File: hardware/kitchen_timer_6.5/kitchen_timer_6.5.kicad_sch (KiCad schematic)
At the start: 58 parts, among them J1 JST PH 2.0, J2 USB_C, J3 BREAKOUT, Q1 MMBT2222A, Q2 MMBT2222A, Q3 MMBT2222A, Q4 MMBT2222A, Q5 MMBT2222A, SW1 ON/OFF, SW2 SECONDS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

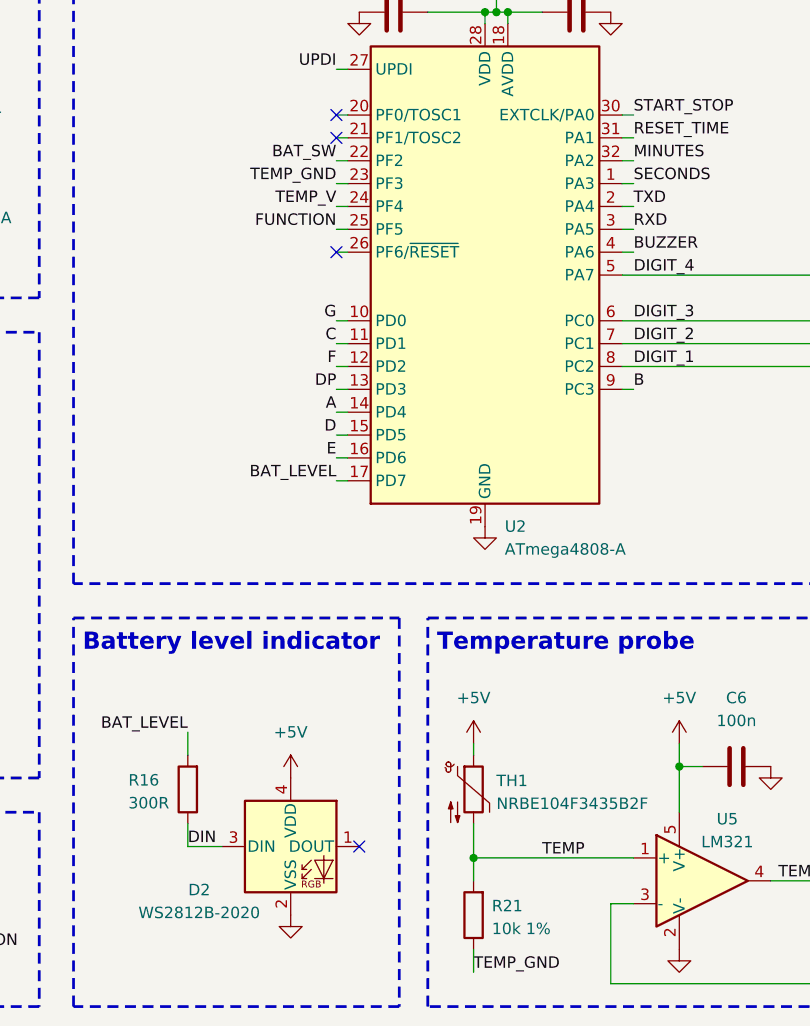
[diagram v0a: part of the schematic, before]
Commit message: converted temp_gnd to temp_vcc and change temperature reading logic
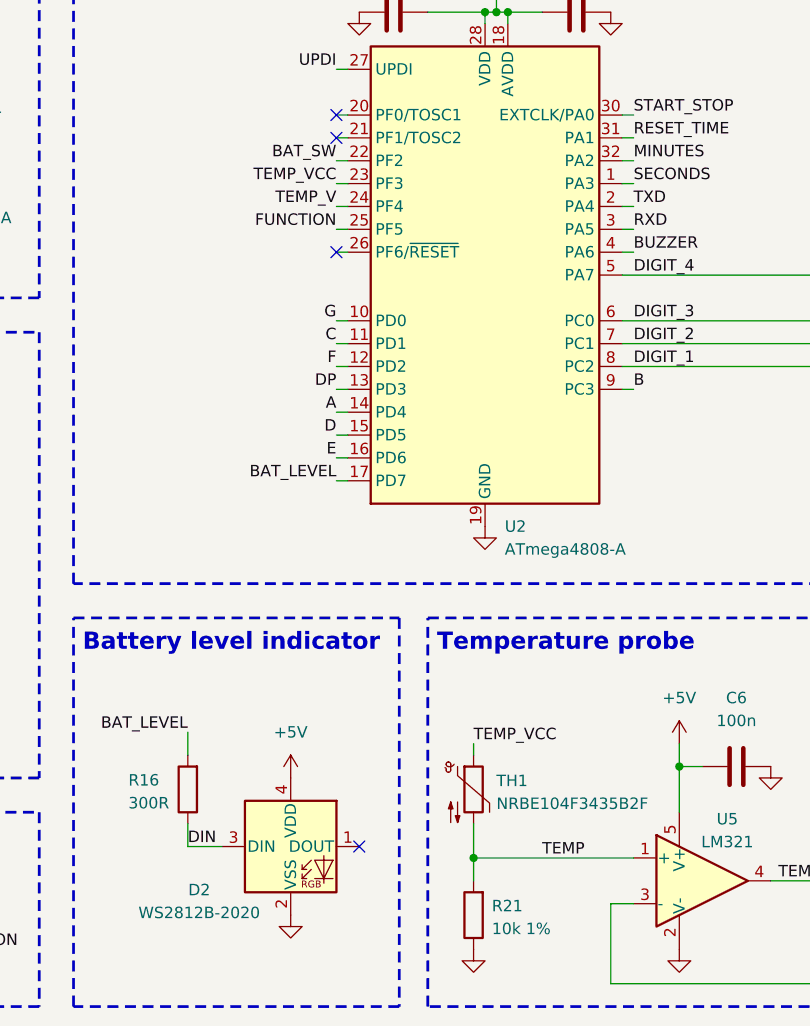
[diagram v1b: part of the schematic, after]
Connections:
- net +5V: no longer TH1.1
- net GND: now also R21.1
- net TEMP_GND renamed TEMP_VCC
- net TEMP_VCC: now also TH1.1; no longer R21.1
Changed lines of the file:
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@@
 	(wire
 		(pts
-			(xy 130.81 187.96) (xy 130.81 190.5)
-		)
-		(stroke
-			(width 0)
-			(type default)
-		)
-	)
-	(wire
-		(pts
 			(xy 132.08 83.82) (xy 133.35 83.82)
 		)
@@
 		)
 	)
-	(label "TEMP_GND"
+	(label "TEMP_VCC"
 		(at 115.57 102.87 180)
 		(effects
@@
 		)
 	)
-	(label "TEMP_GND"
-		(at 130.81 190.5 0)
+	(label "TEMP_VCC"
+		(at 130.81 165.1 0)
 		(effects
 			(font
@@
 	)
 	(symbol
-		(lib_id "00_local:+5V")
-		(at 130.81 165.1 0)
-		(unit 1)
-		(exclude_from_sim no)
-		(in_bom yes)
-		(on_board yes)
-		(dnp no)
-		(fields_autoplaced yes)
-		(property "Reference" "#PWR024"
-			(at 130.81 168.91 0)
-			(effects
-				(font
-					(size 1.27 1.27)
-				)
-				(hide yes)
-			)
-		)
-		(property "Value" "+5V"
-			(at 130.81 160.02 0)
-			(effects
-				(font
-					(size 1.27 1.27)
-				)
-			)
-		)
-		(property "Footprint" ""
-			(at 130.81 165.1 0)
-			(effects
-				(font
-					(size 1.27 1.27)
-				)
-				(hide yes)
-			)
-		)
-		(property "Datasheet" ""
-			(at 130.81 165.1 0)
-			(effects
-				(font
-					(size 1.27 1.27)
-				)
-				(hide yes)
-			)
-		)
-		(property "Description" "Power symbol creates a global label with name \"+5V\""
-			(at 130.81 165.1 0)
-			(effects
-				(font
-					(size 1.27 1.27)
-				)
-				(hide yes)
-			)
-		)
-		(pin "1"
-		)
-		(instances
-			(project "timer_v6.0"
-				(path "/913bc5dc-ca18-41a4-a86c-40ef688df58f"
-					(reference "#PWR024")
-					(unit 1)
-				)
-			)
-		)
-	)
-	(symbol
 		(lib_id "00_local:R")
 		(at 99.06 40.64 270)
@@
 					(unit 1)
 				)
+			)
+		)
+	)
+	(symbol
+		(lib_id "00_local:GND")
+		(at 130.81 187.96 0)
+		(unit 1)
+		(exclude_from_sim no)
+		(in_bom yes)
+		(on_board yes)
+		(dnp no)
+		(fields_autoplaced yes)
+		(property "Reference" "#PWR032"
+			(at 130.81 194.31 0)
+			(effects
+				(font
+					(size 1.27 1.27)
+				)
+				(hide yes)
+			)
+		)
+		(property "Value" "GND"
+			(at 130.81 193.04 0)
+			(effects
+				(font
+					(size 1.27 1.27)
+				)
+				(hide yes)
+			)
+		)
+		(property "Footprint" ""
+			(at 130.81 187.96 0)
+			(effects
+				(font
+					(size 1.27 1.27)
+				)
+				(hide yes)
+			)
+		)
+		(property "Datasheet" ""
+			(at 130.81 187.96 0)
+			(effects
+				(font
+					(size 1.27 1.27)
+				)
+				(hide yes)
+			)
+		)
+		(property "Description" "Power symbol creates a global label with name \"GND\" , ground"
+			(at 130.81 187.96 0)
+			(effects
+				(font
+					(size 1.27 1.27)
+				)
+				(hide yes)
+			)
+		)
+		(pin "1"
+		)
+		(instances
+			(project "kitchen_timer_6.5"
+				(path "/913bc5dc-ca18-41a4-a86c-40ef688df58f"
+					(reference "#PWR032")
+					(unit 1)
+				)
